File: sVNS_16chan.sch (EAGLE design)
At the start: 56 parts, among them IC2 OPA990IDCKR, IC3 EFM8SB10F2G-A-QFN20, J1 M50-3631042, J2 M50-3631042, J3 M50-3631042, U1 NT3H2211W0FHKH, U2 LT8410EDC-1#TRMPBF, U3 MUX36S16IRSNR, U4 MUX36S16IRSNR

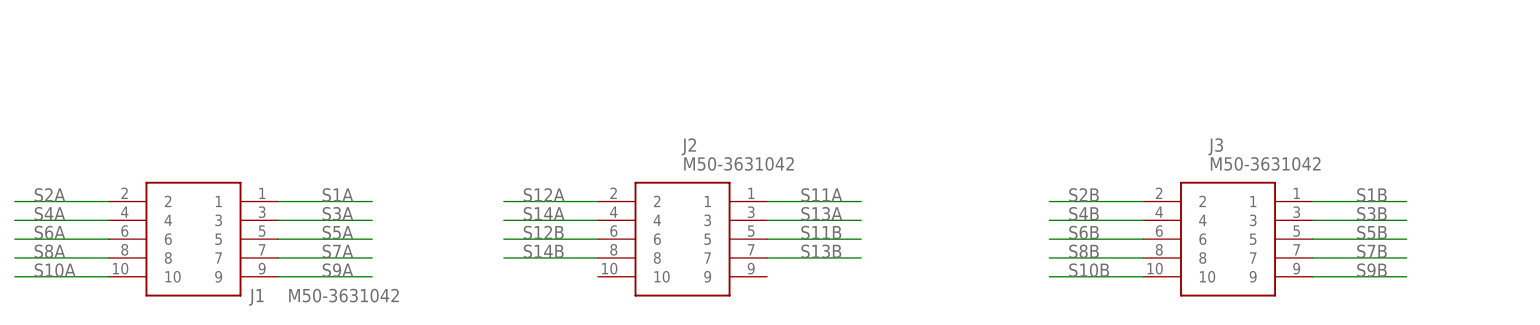
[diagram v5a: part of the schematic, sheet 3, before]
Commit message: Checkpoint 4. Output stage pin nets removed.
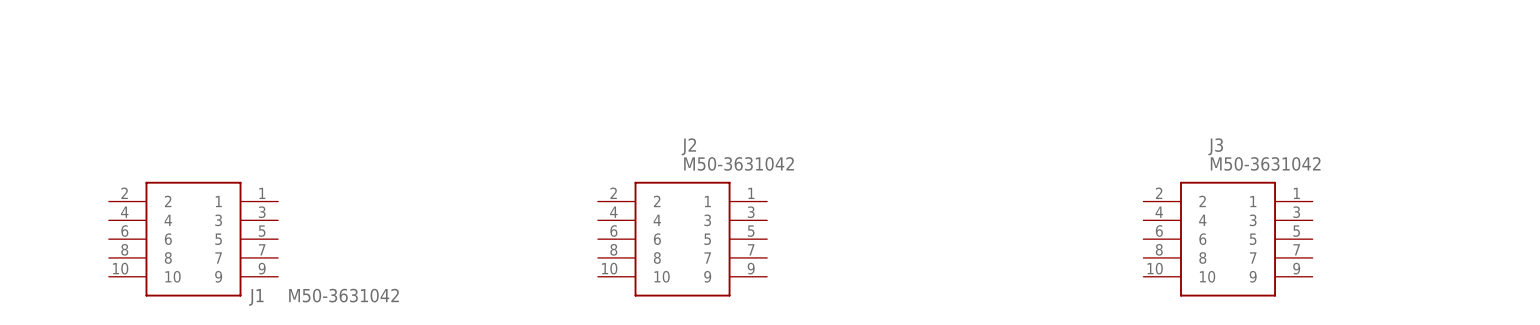
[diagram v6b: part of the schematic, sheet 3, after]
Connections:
- net S10A: no longer J1.10
- net S10B: no longer J3.10
- net S11A: no longer J2.1
- net S11B: no longer J2.5
- net S12A: no longer J2.2
- net S12B: no longer J2.6
- net S13A: no longer J2.3
- net S13B: no longer J2.7
- net S14A: no longer J2.4
- net S14B: no longer J2.8
- net S1A: no longer J1.1
- net S1B: no longer J3.1
- net S2A: no longer J1.2
- net S2B: no longer J3.2
- net S3A: no longer J1.3
- net S3B: no longer J3.3
- net S4A: no longer J1.4
- net S4B: no longer J3.4
- net S5A: no longer J1.5
- net S5B: no longer J3.5
- net S6A: no longer J1.6
- net S6B: no longer J3.6
- net S7A: no longer J1.7
- net S7B: no longer J3.7
- net S8A: no longer J1.8
- net S8B: no longer J3.8
- net S9A: no longer J1.9
- net S9B: no longer J3.9
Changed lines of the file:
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@@
 <label x="73.66" y="96.52" size="1.778" layer="95"/>
-</segment>
-<segment>
-<pinref part="J2" gate="G$1" pin="4"/>
-<wire x1="99.06" y1="40.64" x2="86.36" y2="40.64" width="0.1524" layer="91"/>
-<label x="88.9" y="40.64" size="1.778" layer="95"/>
 </segment>
 </net>
@@
 <label x="71.12" y="99.06" size="1.778" layer="95"/>
 </segment>
-<segment>
-<pinref part="J2" gate="G$1" pin="3"/>
-<wire x1="121.92" y1="40.64" x2="134.62" y2="40.64" width="0.1524" layer="91"/>
-<label x="132.08" y="40.64" size="1.778" layer="95" align="bottom-right"/>
-</segment>
 </net>
 <net name="S12A" class="0">
@@
 <label x="68.58" y="101.6" size="1.778" layer="95"/>
 </segment>
-<segment>
-<pinref part="J2" gate="G$1" pin="2"/>
-<wire x1="99.06" y1="43.18" x2="86.36" y2="43.18" width="0.1524" layer="91"/>
-<label x="88.9" y="43.18" size="1.778" layer="95"/>
-</segment>
 </net>
 <net name="S11A" class="0">
@@
 <label x="66.04" y="104.14" size="1.778" layer="95"/>
 </segment>
-<segment>
-<pinref part="J2" gate="G$1" pin="1"/>
-<wire x1="121.92" y1="43.18" x2="134.62" y2="43.18" width="0.1524" layer="91"/>
-<label x="132.08" y="43.18" size="1.778" layer="95" align="bottom-right"/>
-</segment>
 </net>
 <net name="S10A" class="0">
@@
 <label x="63.5" y="106.68" size="1.778" layer="95"/>
 </segment>
-<segment>
-<pinref part="J1" gate="G$1" pin="10"/>
-<wire x1="33.02" y1="33.02" x2="20.32" y2="33.02" width="0.1524" layer="91"/>
-<label x="22.86" y="33.02" size="1.778" layer="95"/>
-</segment>
 </net>
 <net name="S9A" class="0">
@@
 <label x="60.96" y="109.22" size="1.778" layer="95"/>
 </segment>
-<segment>
-<pinref part="J1" gate="G$1" pin="9"/>
-<wire x1="55.88" y1="33.02" x2="68.58" y2="33.02" width="0.1524" layer="91"/>
-<label x="66.04" y="33.02" size="1.778" layer="95" align="bottom-right"/>
-</segment>
 </net>
 <net name="S8A" class="0">
@@
 <label x="60.96" y="111.76" size="1.778" layer="95"/>
 </segment>
-<segment>
-<pinref part="J1" gate="G$1" pin="8"/>
-<wire x1="33.02" y1="35.56" x2="20.32" y2="35.56" width="0.1524" layer="91"/>
-<label x="22.86" y="35.56" size="1.778" layer="95"/>
-</segment>
 </net>
 <net name="S7A" class="0">
@@
 <label x="60.96" y="114.3" size="1.778" layer="95"/>
 </segment>
-<segment>
-<pinref part="J1" gate="G$1" pin="7"/>
-<wire x1="55.88" y1="35.56" x2="68.58" y2="35.56" width="0.1524" layer="91"/>
-<label x="66.04" y="35.56" size="1.778" layer="95" align="bottom-right"/>
-</segment>
 </net>
 <net name="S6A" class="0">
@@
 <label x="60.96" y="116.84" size="1.778" layer="95"/>
 </segment>
-<segment>
-<pinref part="J1" gate="G$1" pin="6"/>
-<wire x1="33.02" y1="38.1" x2="20.32" y2="38.1" width="0.1524" layer="91"/>
-<label x="22.86" y="38.1" size="1.778" layer="95"/>
-</segment>
 </net>
 <net name="S5A" class="0">
@@
 <label x="60.96" y="119.38" size="1.778" layer="95"/>
 </segment>
-<segment>
-<pinref part="J1" gate="G$1" pin="5"/>
-<wire x1="55.88" y1="38.1" x2="68.58" y2="38.1" width="0.1524" layer="91"/>
-<label x="66.04" y="38.1" size="1.778" layer="95" align="bottom-right"/>
-</segment>
 </net>
 <net name="S4A" class="0">
@@
 <label x="60.96" y="121.92" size="1.778" layer="95"/>
 </segment>
-<segment>
-<pinref part="J1" gate="G$1" pin="4"/>
-<wire x1="33.02" y1="40.64" x2="20.32" y2="40.64" width="0.1524" layer="91"/>
-<label x="22.86" y="40.64" size="1.778" layer="95"/>
-</segment>
 </net>
 <net name="S3A" class="0">
@@
 <label x="60.96" y="124.46" size="1.778" layer="95"/>
 </segment>
-<segment>
-<pinref part="J1" gate="G$1" pin="3"/>
-<wire x1="55.88" y1="40.64" x2="68.58" y2="40.64" width="0.1524" layer="91"/>
-<label x="66.04" y="40.64" size="1.778" layer="95" align="bottom-right"/>
-</segment>
 </net>
 <net name="S2A" class="0">
@@
 <label x="60.96" y="127" size="1.778" layer="95"/>
 </segment>
-<segment>
-<pinref part="J1" gate="G$1" pin="2"/>
-<wire x1="33.02" y1="43.18" x2="20.32" y2="43.18" width="0.1524" layer="91"/>
-<label x="22.86" y="43.18" size="1.778" layer="95"/>
-</segment>
 </net>
 <net name="S1A" class="0">
@@
 <label x="60.96" y="129.54" size="1.778" layer="95"/>
 </segment>
-<segment>
-<pinref part="J1" gate="G$1" pin="1"/>
-<wire x1="55.88" y1="43.18" x2="68.58" y2="43.18" width="0.1524" layer="91"/>
-<label x="66.04" y="43.18" size="1.778" layer="95" align="bottom-right"/>
-</segment>
 </net>
 <net name="S16B" class="0">
@@
 <label x="170.18" y="96.52" size="1.778" layer="95"/>
 </segment>
-<segment>
-<pinref part="J2" gate="G$1" pin="8"/>
-<wire x1="99.06" y1="35.56" x2="86.36" y2="35.56" width="0.1524" layer="91"/>
-<label x="88.9" y="35.56" size="1.778" layer="95"/>
-</segment>
 </net>
 <net name="S13B" class="0">
@@
 <label x="167.64" y="99.06" size="1.778" layer="95"/>
 </segment>
-<segment>
-<pinref part="J2" gate="G$1" pin="7"/>
-<wire x1="121.92" y1="35.56" x2="134.62" y2="35.56" width="0.1524" layer="91"/>
-<label x="132.08" y="35.56" size="1.778" layer="95" align="bottom-right"/>
-</segment>
 </net>
 <net name="S12B" class="0">
@@
 <label x="165.1" y="101.6" size="1.778" layer="95"/>
 </segment>
-<segment>
-<pinref part="J2" gate="G$1" pin="6"/>
-<wire x1="99.06" y1="38.1" x2="86.36" y2="38.1" width="0.1524" layer="91"/>
-<label x="88.9" y="38.1" size="1.778" layer="95"/>
-</segment>
 </net>
 <net name="S11B" class="0">
@@
 <label x="162.56" y="104.14" size="1.778" layer="95"/>
 </segment>
-<segment>
-<pinref part="J2" gate="G$1" pin="5"/>
-<wire x1="121.92" y1="38.1" x2="134.62" y2="38.1" width="0.1524" layer="91"/>
-<label x="132.08" y="38.1" size="1.778" layer="95" align="bottom-right"/>
-</segment>
 </net>
 <net name="S10B" class="0">
@@
 <label x="160.02" y="106.68" size="1.778" layer="95"/>
 </segment>
-<segment>
-<pinref part="J3" gate="G$1" pin="10"/>
-<wire x1="172.72" y1="33.02" x2="160.02" y2="33.02" width="0.1524" layer="91"/>
-<label x="162.56" y="33.02" size="1.778" layer="95"/>
-</segment>
 </net>
 <net name="S9B" class="0">
@@
 <label x="157.48" y="109.22" size="1.778" layer="95"/>
 </segment>
-<segment>
-<pinref part="J3" gate="G$1" pin="9"/>
-<wire x1="195.58" y1="33.02" x2="208.28" y2="33.02" width="0.1524" layer="91"/>
-<label x="205.74" y="33.02" size="1.778" layer="95" align="bottom-right"/>
-</segment>
 </net>
 <net name="S8B" class="0">
@@
 <label x="157.48" y="111.76" size="1.778" layer="95"/>
 </segment>
-<segment>
-<pinref part="J3" gate="G$1" pin="8"/>
-<wire x1="172.72" y1="35.56" x2="160.02" y2="35.56" width="0.1524" layer="91"/>
-<label x="162.56" y="35.56" size="1.778" layer="95"/>
-</segment>
 </net>
 <net name="S7B" class="0">
@@
 <label x="157.48" y="114.3" size="1.778" layer="95"/>
 </segment>
-<segment>
-<pinref part="J3" gate="G$1" pin="7"/>
-<wire x1="195.58" y1="35.56" x2="208.28" y2="35.56" width="0.1524" layer="91"/>
-<label x="205.74" y="35.56" size="1.778" layer="95" align="bottom-right"/>
-</segment>
 </net>
 <net name="S6B" class="0">
@@
 <label x="157.48" y="116.84" size="1.778" layer="95"/>
 </segment>
-<segment>
-<pinref part="J3" gate="G$1" pin="6"/>
-<wire x1="172.72" y1="38.1" x2="160.02" y2="38.1" width="0.1524" layer="91"/>
-<label x="162.56" y="38.1" size="1.778" layer="95"/>
-</segment>
 </net>
 <net name="S5B" class="0">
@@
 <label x="157.48" y="119.38" size="1.778" layer="95"/>
 </segment>
-<segment>
-<pinref part="J3" gate="G$1" pin="5"/>
-<wire x1="195.58" y1="38.1" x2="208.28" y2="38.1" width="0.1524" layer="91"/>
-<label x="205.74" y="38.1" size="1.778" layer="95" align="bottom-right"/>
-</segment>
 </net>
 <net name="S4B" class="0">
@@
 <label x="157.48" y="121.92" size="1.778" layer="95"/>
 </segment>
-<segment>
-<pinref part="J3" gate="G$1" pin="4"/>
-<wire x1="172.72" y1="40.64" x2="160.02" y2="40.64" width="0.1524" layer="91"/>
-<label x="162.56" y="40.64" size="1.778" layer="95"/>
-</segment>
 </net>
 <net name="S3B" class="0">
@@
 <label x="157.48" y="124.46" size="1.778" layer="95"/>
 </segment>
-<segment>
-<pinref part="J3" gate="G$1" pin="3"/>
-<wire x1="195.58" y1="40.64" x2="208.28" y2="40.64" width="0.1524" layer="91"/>
-<label x="205.74" y="40.64" size="1.778" layer="95" align="bottom-right"/>
-</segment>
 </net>
 <net name="S2B" class="0">
@@
 <label x="157.48" y="127" size="1.778" layer="95"/>
 </segment>
-<segment>
-<pinref part="J3" gate="G$1" pin="2"/>
-<wire x1="172.72" y1="43.18" x2="160.02" y2="43.18" width="0.1524" layer="91"/>
-<label x="162.56" y="43.18" size="1.778" layer="95"/>
-</segment>
 </net>
 <net name="S1B" class="0">
@@
 <label x="157.48" y="129.54" size="1.778" layer="95"/>
 </segment>
-<segment>
-<pinref part="J3" gate="G$1" pin="1"/>
-<wire x1="195.58" y1="43.18" x2="208.28" y2="43.18" width="0.1524" layer="91"/>
-<label x="205.74" y="43.18" size="1.778" layer="95" align="bottom-right"/>
-</segment>
-</net>
+</net>

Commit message: Checkpoint 5. Closer to success?
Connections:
- net +3.3V: now also R23.1; no longer L1.1, R23.2, U2.VCC
- net +3.3V_LT8410_VCC: now also L1.1, R23.2, U2.VCC; no longer R23.1
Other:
- moved on the sheet: R23
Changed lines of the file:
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@@
 <part name="R19" library="sVNS_16chan_lib" deviceset="SMD_PADS_0603" device="" package3d_urn="urn:adsk.eagle:package:23555/3"/>
 <part name="R20" library="sVNS_16chan_lib" deviceset="SMD_PADS_0603" device="" package3d_urn="urn:adsk.eagle:package:23555/3"/>
-<part name="R23" library="sVNS_16chan_lib" deviceset="SMD_PADS_0603" device="" package3d_urn="urn:adsk.eagle:package:23555/3"/>
 <part name="R24" library="sVNS_16chan_lib" deviceset="SMD_PADS_0603" device="" package3d_urn="urn:adsk.eagle:package:23555/3"/>
 <part name="R25" library="sVNS_16chan_lib" deviceset="SMD_PADS_0603" device="" package3d_urn="urn:adsk.eagle:package:23555/3"/>
@@
 <part name="R29" library="rcl" library_urn="urn:adsk.eagle:library:334" deviceset="R-EU_" device="R0402" package3d_urn="urn:adsk.eagle:package:23547/3" value="1.3M"/>
 <part name="R30" library="sVNS_16chan_lib" deviceset="SMD_PADS_0603" device="" package3d_urn="urn:adsk.eagle:package:23555/3"/>
+<part name="R23" library="sVNS_16chan_lib" deviceset="SMD_PADS_0603" device="" package3d_urn="urn:adsk.eagle:package:23555/3"/>
 </parts>
 <sheets>
@@
 <attribute name="VALUE" x="131.064" y="76.581" size="1.778" layer="96"/>
 </instance>
-<instance part="R23" gate="G$1" x="50.8" y="73.66" smashed="yes">
-<attribute name="NAME" x="50.038" y="74.6506" size="1.27" layer="95"/>
-<attribute name="VALUE" x="46.99" y="70.358" size="1.778" layer="96"/>
-</instance>
 <instance part="R24" gate="G$1" x="30.48" y="22.86" smashed="yes" rot="R90">
 <attribute name="NAME" x="29.4894" y="22.098" size="1.27" layer="95" rot="R90"/>
@@
 <attribute name="NAME" x="130.302" y="143.7894" size="1.27" layer="95" rot="R180"/>
 <attribute name="VALUE" x="133.35" y="148.082" size="1.778" layer="96" rot="R180"/>
+</instance>
+<instance part="R23" gate="G$1" x="53.34" y="88.9" smashed="yes">
+<attribute name="NAME" x="52.578" y="89.8906" size="1.27" layer="95"/>
+<attribute name="VALUE" x="49.53" y="85.598" size="1.778" layer="96"/>
 </instance>
 </instances>
@@
 </segment>
 <segment>
-<junction x="58.42" y="73.66"/>
-<wire x1="58.42" y1="73.66" x2="58.42" y2="88.9" width="0.1524" layer="91"/>
-<pinref part="L1" gate="G$1" pin="1"/>
-<wire x1="58.42" y1="68.58" x2="58.42" y2="73.66" width="0.1524" layer="91"/>
-<label x="58.42" y="88.9" size="1.778" layer="95"/>
-<pinref part="U2" gate="G$1" pin="VCC"/>
-<wire x1="58.42" y1="73.66" x2="71.12" y2="73.66" width="0.1524" layer="91"/>
-<wire x1="58.42" y1="73.66" x2="55.88" y2="73.66" width="0.1524" layer="91"/>
-<pinref part="R23" gate="G$1" pin="2"/>
-</segment>
-<segment>
 <pinref part="R26" gate="G$1" pin="2"/>
 <wire x1="10.16" y1="147.32" x2="10.16" y2="149.86" width="0.1524" layer="91"/>
 <label x="7.62" y="149.86" size="1.778" layer="95"/>
+</segment>
+<segment>
+<pinref part="R23" gate="G$1" pin="1"/>
+<wire x1="48.26" y1="88.9" x2="43.18" y2="88.9" width="0.1524" layer="91"/>
+<label x="43.18" y="88.9" size="1.778" layer="95"/>
 </segment>
 </net>
@@
 </segment>
 </net>
-<net name="+3.3V_LT8410_VCC" class="0">
-<segment>
-<pinref part="C1" gate="G$1" pin="2"/>
-<wire x1="43.18" y1="73.66" x2="45.72" y2="73.66" width="0.1524" layer="91"/>
-<pinref part="R23" gate="G$1" pin="1"/>
-<label x="42.164" y="70.866" size="0.6096" layer="95"/>
-</segment>
-</net>
 <net name="+3.3V_PIN" class="0">
 <segment>
@@
 </segment>
 </net>
+<net name="+3.3V_LT8410_VCC" class="0">
+<segment>
+<junction x="58.42" y="73.66"/>
+<wire x1="58.42" y1="73.66" x2="58.42" y2="88.9" width="0.1524" layer="91"/>
+<pinref part="L1" gate="G$1" pin="1"/>
+<wire x1="58.42" y1="68.58" x2="58.42" y2="73.66" width="0.1524" layer="91"/>
+<label x="58.42" y="88.9" size="1.778" layer="95"/>
+<pinref part="U2" gate="G$1" pin="VCC"/>
+<wire x1="58.42" y1="73.66" x2="71.12" y2="73.66" width="0.1524" layer="91"/>
+<pinref part="R23" gate="G$1" pin="2"/>
+<pinref part="C1" gate="G$1" pin="2"/>
+<label x="42.164" y="70.866" size="0.6096" layer="95"/>
+<wire x1="58.42" y1="73.66" x2="43.18" y2="73.66" width="0.1524" layer="91"/>
+</segment>
+</net>
